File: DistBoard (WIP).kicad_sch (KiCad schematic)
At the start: 43 parts, among them J1 22-27-2021, J10 Conn_01x03, J11 Conn_01x03, J12 Conn_01x03, J13 Conn_01x03, J14 PPTC241LFBN-RC, J15 PPTC241LFBN-RC, J2 Conn_01x03, J3 Conn_01x03, J4 Conn_01x03, J5 Conn_01x03, J6 Conn_01x03, J7 Conn_01x03, J8 Conn_01x03, J9 Conn_01x03, U1 TLE2426CDR

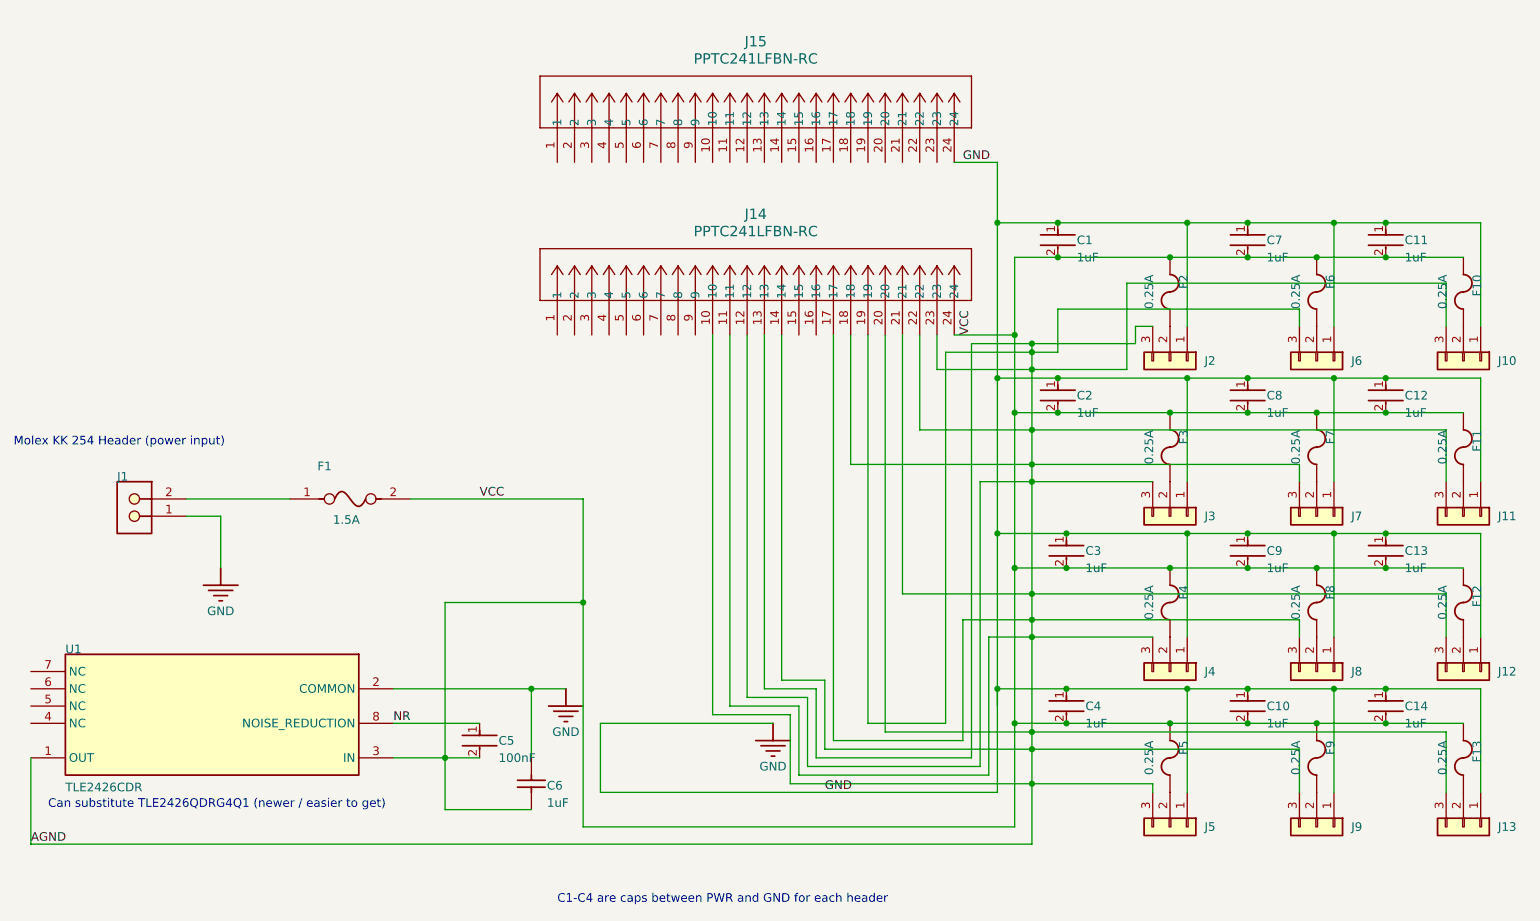
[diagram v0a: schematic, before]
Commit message: Changed PCB to correct spacing on all headers and corrected routes to FPGA headers. Changed schematic to include net labels instead of physical wires and corrected routing from single channel boards to FPGA headers.
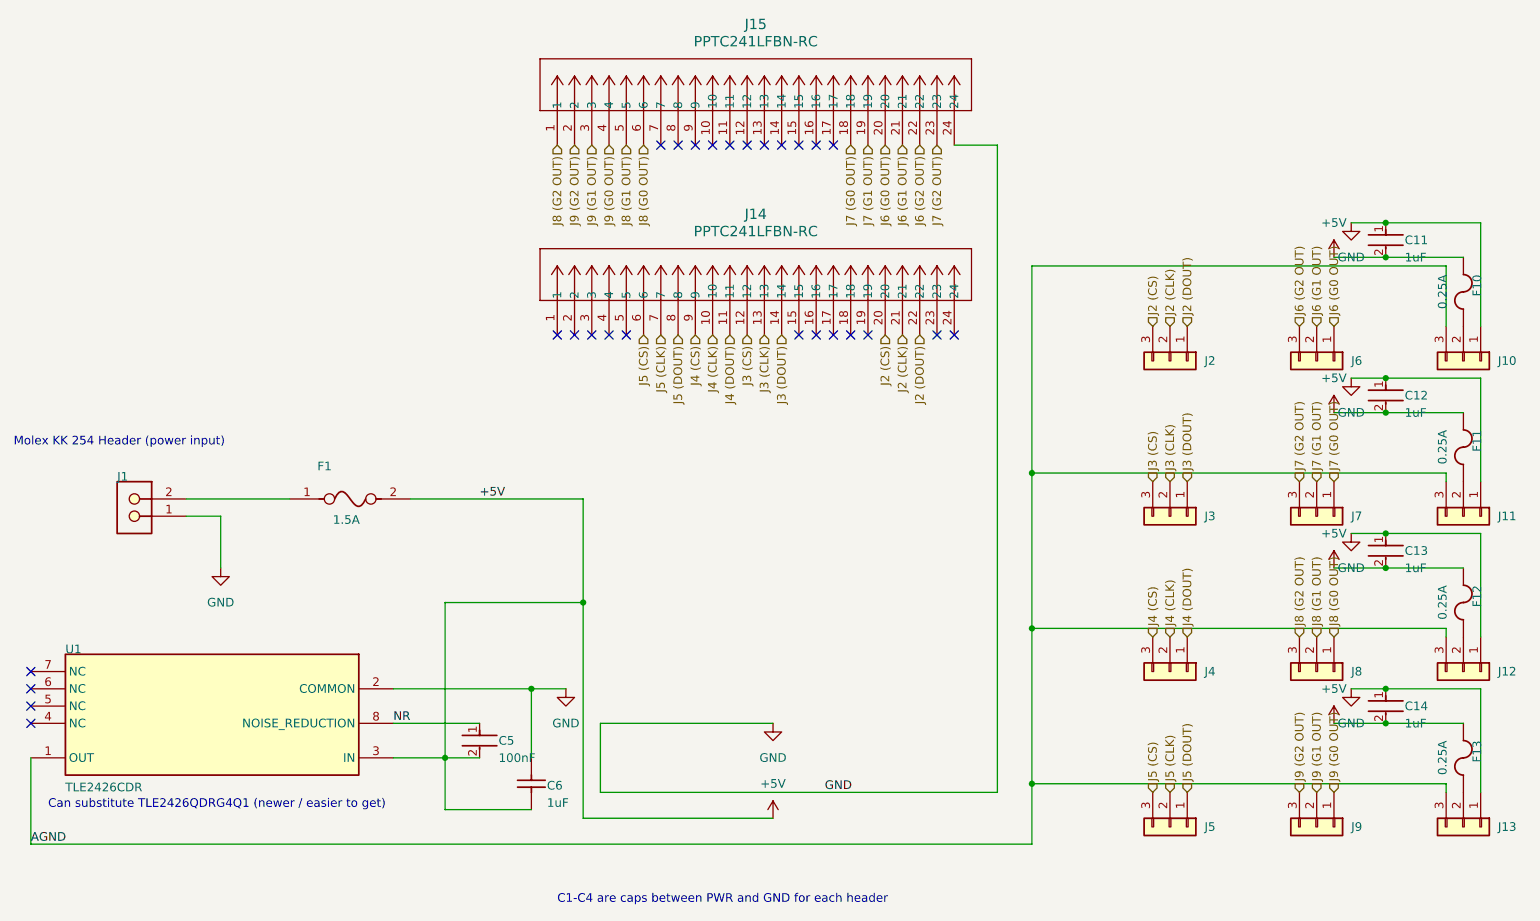
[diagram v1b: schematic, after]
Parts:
- removed C1, C10, C2, C3, C4, C7, C8, C9: 1uF, Capacitor_SMD:C_0805_2012Metric_Pad1.18x1.45mm_HandSolder, symbol DistBoard-altium-import:root_0_02cd4be3c70576c341d710602a673aa
- removed F2, F3, F4, F5, F6, F7, F8, F9: 0.25A, AltiumImport:LFUS-459_V, symbol DistBoard-altium-import:root_0_FUSE-2
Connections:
- net AGND: no longer J14.10, J14.11, J14.12, J14.13, J14.14, J14.17, J14.18, J14.19, J14.20, J14.21, J14.22, J14.23, J2.3 (Pin_3), J3.3 (Pin_3), J4.3 (Pin_3), J5.3 (Pin_3), J6.3 (Pin_3), J7.3 (Pin_3), J8.3 (Pin_3), J9.3 (Pin_3)
- net GND: no longer J2.1 (Pin_1), J3.1 (Pin_1), J4.1 (Pin_1), J5.1 (Pin_1), J6.1 (Pin_1), J7.1 (Pin_1), J8.1 (Pin_1), J9.1 (Pin_1)
- net J4 (CLK): now reaches J4.2 (Pin_2)
- net J4 (CLK): now also J14.10
- net J3 (CLK): now reaches J3.2 (Pin_2)
- net J3 (CLK): now also J14.13
- net J8 (G1 OUT): now reaches J8.2 (Pin_2)
- net J8 (G1 OUT): now also J15.5
- net J5 (CLK): now reaches J5.2 (Pin_2)
- net J5 (CLK): now also J14.7
- net J5 (CS): now reaches J14.6
- net J5 (CS): now also J5.3 (Pin_3)
- net J5 (DOUT): now reaches J14.8
- net J5 (DOUT): now also J5.1 (Pin_1)
- net J4 (CS): now reaches J14.9
- net J4 (CS): now also J4.3 (Pin_3)
- net J2 (CLK): now reaches J2.2 (Pin_2)
- net J2 (CLK): now also J14.21
- net J6 (G1 OUT): now reaches J6.2 (Pin_2)
- net J6 (G1 OUT): now also J15.21
- net J8 (G2 OUT): now reaches J15.1
- net J8 (G2 OUT): now also J8.3 (Pin_3)
- net J7 (G0 OUT): now reaches J15.18
- net J7 (G0 OUT): now also J7.1 (Pin_1)
- net J7 (G1 OUT): now reaches J15.19
- net J7 (G1 OUT): now also J7.2 (Pin_2)
- net J9 (G2 OUT): now reaches J15.2
- net J9 (G2 OUT): now also J9.3 (Pin_3)
- net J6 (G0 OUT): now reaches J15.20
- net J6 (G0 OUT): now also J6.1 (Pin_1)
- net J6 (G2 OUT): now reaches J15.22
- net J6 (G2 OUT): now also J6.3 (Pin_3)
- net J7 (G2 OUT): now reaches J15.23
- net J7 (G2 OUT): now also J7.3 (Pin_3)
- net J9 (G1 OUT): now reaches J15.3
- net J9 (G1 OUT): now also J9.2 (Pin_2)
- net J9 (G0 OUT): now reaches J15.4
- net J9 (G0 OUT): now also J9.1 (Pin_1)
- net J8 (G0 OUT): now reaches J15.6
- net J8 (G0 OUT): now also J8.1 (Pin_1)
- net VCC renamed +5V
- net +5V: no longer J14.24
- new net J2 (CS): J14.20, J2.3 (Pin_3)
- new net J2 (DOUT): J14.22, J2.1 (Pin_1)
- new net J3 (CS): J14.12, J3.3 (Pin_3)
- new net J3 (DOUT): J14.14, J3.1 (Pin_1)
- new net J4 (DOUT): J14.11, J4.1 (Pin_1)
- no-connect marks 0 -> 27
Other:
- moved on the sheet: J15
